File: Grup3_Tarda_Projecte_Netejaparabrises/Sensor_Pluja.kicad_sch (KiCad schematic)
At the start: 5 parts, among them J7 CONEXIOSENSOR, U2 LM393

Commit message: canvis reles
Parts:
- RPOT1: footprint Resistor_SMD:R_0805_2012Metric_Pad1.20x1.40mm_HandSolder -> Projecte:TRIM_3362P-1-103
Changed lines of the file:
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@@
       (effects (font (size 1.27 1.27)) (justify right))
     )
-    (property "Footprint" "Resistor_SMD:R_0805_2012Metric_Pad1.20x1.40mm_HandSolder" (at 110.744 106.68 0)
+    (property "Footprint" "Projecte:TRIM_3362P-1-103" (at 110.744 106.68 0)
       (effects (font (size 1.27 1.27)) hide)
     )

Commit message: Layout 3
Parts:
- CDesOpam1: footprint Capacitor_SMD:CP_Elec_4x3 -> Capacitor_SMD:C_0805_2012Metric
- RPOT1: footprint Projecte:TRIM_3362P-1-103 -> POTENCIOMETRE:TRIM_3362P-1-103
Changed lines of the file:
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@@
   (title_block
     (title "Projecte Netejaparabrises - Grup 4 Tarda")
-    (date "2023-04-12")
-    (rev "v1.2.12042023")
+    (date "2023-04-05")
+    (rev "v1.1.05042023")
   )
   (junction (at 110.744 99.06) (diameter 0) (color 0 0 0 0)
@@
       (effects (font (size 1.27 1.27)) (justify right))
     )
-    (property "Footprint" "Projecte:TRIM_3362P-1-103" (at 110.744 106.68 0)
+    (property "Footprint" "POTENCIOMETRE:TRIM_3362P-1-103" (at 110.744 106.68 0)
       (effects (font (size 1.27 1.27)) hide)
     )
@@
       (effects (font (size 1.27 1.27)) (justify left))
     )
-    (property "Footprint" "Capacitor_SMD:CP_Elec_4x3" (at 177.4952 107.442 0)
-      (effects (font (size 1.27 1.27)) hide)
-    )
+    (property "Footprint" "Capacitor_SMD:C_0805_2012Metric" (at 177.4952 107.442 0)
+      (effects (font (size 1.27 1.27)) hide)
+    )

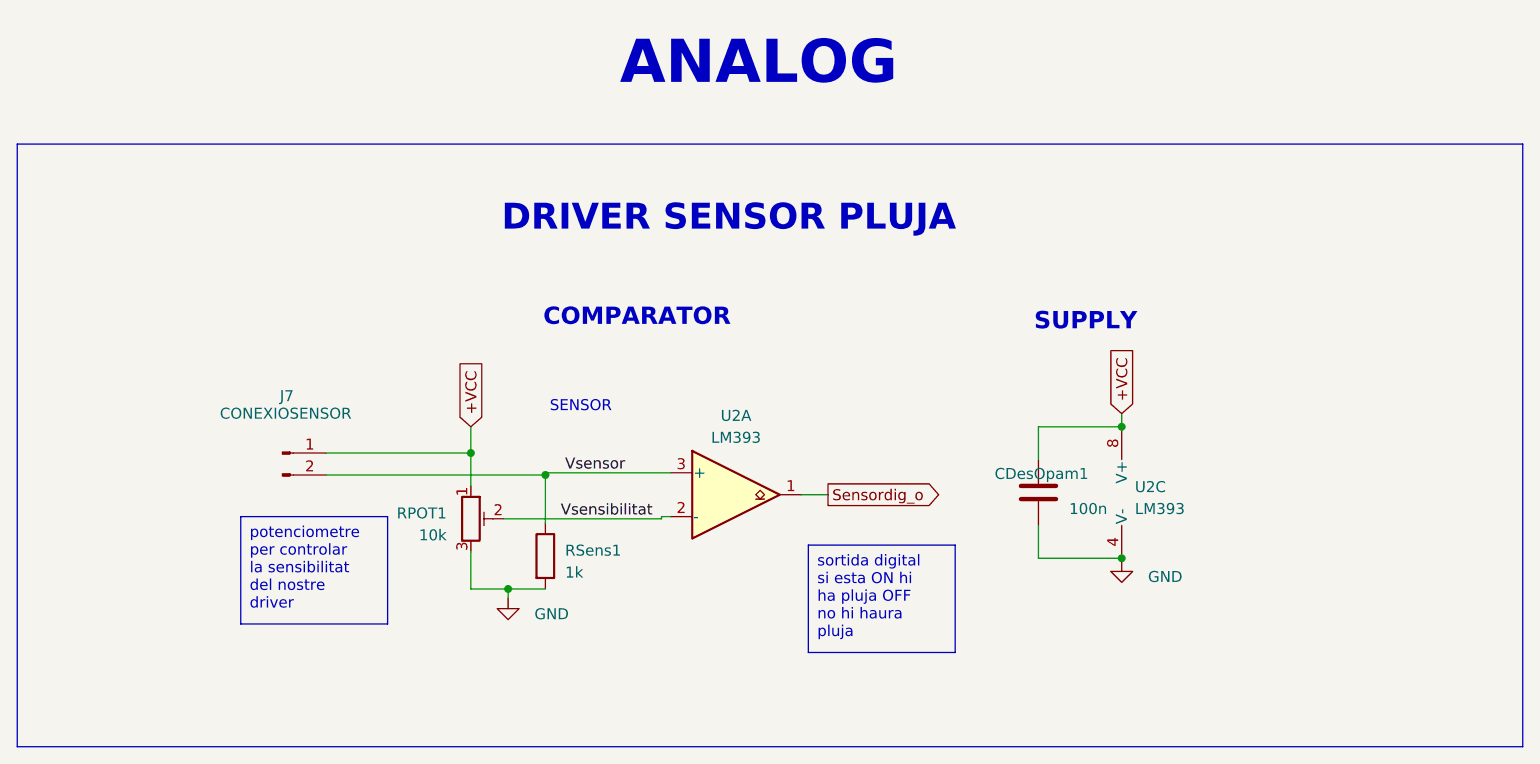
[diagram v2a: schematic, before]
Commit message: canvis divisor sensor de pluja, node vbat protegit, connector de motors, README
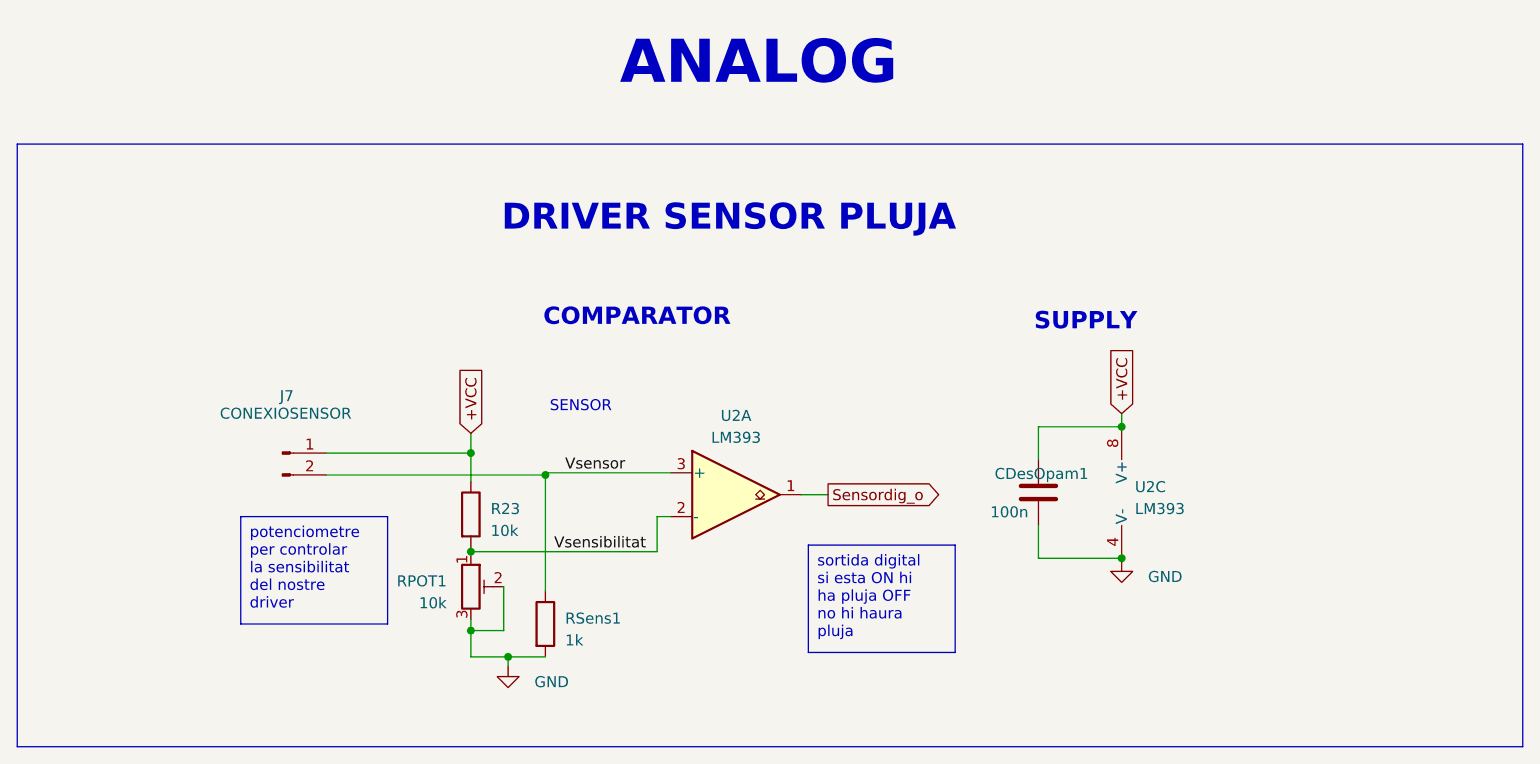
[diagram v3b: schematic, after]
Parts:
- added R23: 10k, Resistor_SMD:R_0805_2012Metric_Pad1.20x1.40mm_HandSolder, symbol Device:R
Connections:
- net +VCC: now also R23.1; no longer RPOT1.1
- net GND: now also RPOT1.2
- net Vsensibilitat: now also RPOT1.1, R23.2; no longer RPOT1.2
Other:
- moved on the sheet: RPOT1, RSens1
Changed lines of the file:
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@@
   (junction (at 110.744 99.06) (diameter 0) (color 0 0 0 0)
   )
+  (junction (at 110.744 119.634) (diameter 0) (color 0 0 0 0)
+  )
   (junction (at 119.38 101.6) (diameter 0) (color 0 0 0 0)
   )
@@
   (junction (at 186.182 111.252) (diameter 0) (color 0 0 0 0)
   )
-  (junction (at 115.062 114.808) (diameter 0) (color 0 0 0 0)
-  )
-  (wire (pts (xy 93.98 99.06) (xy 110.744 99.06))
-    (stroke (width 0) (type default))
-  )
-  (wire (pts (xy 115.062 114.808) (xy 119.38 114.808))
+  (junction (at 110.744 110.49) (diameter 0) (color 0 0 0 0)
+  )
+  (junction (at 115.062 122.682) (diameter 0) (color 0 0 0 0)
+  )
+  (wire (pts (xy 115.062 122.682) (xy 119.38 122.682))
+    (stroke (width 0) (type default))
+  )
+  (wire (pts (xy 114.554 114.554) (xy 114.554 119.634))
     (stroke (width 0) (type default))
   )
@@
     (stroke (width 0) (type default))
   )
-  (wire (pts (xy 110.744 96.012) (xy 110.744 99.06))
+  (wire (pts (xy 110.744 96.774) (xy 110.744 99.06))
     (stroke (width 0) (type default))
   )
@@
     (stroke (width 0) (type default))
   )
-  (wire (pts (xy 115.062 114.808) (xy 115.062 115.824))
-    (stroke (width 0) (type default))
-  )
-  (wire (pts (xy 132.842 106.68) (xy 114.554 106.68))
-    (stroke (width 0) (type default))
-  )
-  (wire (pts (xy 110.744 114.808) (xy 115.062 114.808))
-    (stroke (width 0) (type default))
-  )
-  (wire (pts (xy 132.842 106.426) (xy 132.842 106.68))
-    (stroke (width 0) (type default))
-  )
-  (wire (pts (xy 110.744 110.49) (xy 110.744 114.808))
+  (wire (pts (xy 115.062 122.682) (xy 115.062 123.698))
+    (stroke (width 0) (type default))
+  )
+  (wire (pts (xy 110.744 99.06) (xy 93.98 99.06))
+    (stroke (width 0) (type default))
+  )
+  (wire (pts (xy 110.744 110.49) (xy 132.334 110.49))
+    (stroke (width 0) (type default))
+  )
+  (wire (pts (xy 110.744 122.682) (xy 115.062 122.682))
+    (stroke (width 0) (type default))
+  )
+  (wire (pts (xy 110.744 99.06) (xy 110.744 102.362))
+    (stroke (width 0) (type default))
+  )
+  (wire (pts (xy 110.744 119.634) (xy 114.554 119.634))
+    (stroke (width 0) (type default))
+  )
+  (wire (pts (xy 132.334 106.426) (xy 132.334 110.49))
+    (stroke (width 0) (type default))
+  )
+  (wire (pts (xy 110.744 118.364) (xy 110.744 119.634))
     (stroke (width 0) (type default))
   )
@@
     (stroke (width 0) (type default))
   )
-  (wire (pts (xy 119.38 101.6) (xy 119.38 107.188))
+  (wire (pts (xy 110.744 109.982) (xy 110.744 110.49))
+    (stroke (width 0) (type default))
+  )
+  (wire (pts (xy 119.38 101.6) (xy 119.38 115.062))
     (stroke (width 0) (type default))
   )
@@
     (stroke (width 0) (type default))
   )
-  (wire (pts (xy 132.842 106.426) (xy 133.858 106.426))
-    (stroke (width 0) (type default))
-  )
-  (wire (pts (xy 110.744 99.06) (xy 110.744 102.87))
+  (wire (pts (xy 132.334 106.426) (xy 133.858 106.426))
+    (stroke (width 0) (type default))
+  )
+  (wire (pts (xy 110.744 119.634) (xy 110.744 122.682))
     (stroke (width 0) (type default))
   )
@@
   )
   (polyline (pts (xy 232.664 133.096) (xy 58.166 133.096))
+    (stroke (width 0) (type default))
+  )
+  (wire (pts (xy 110.744 110.49) (xy 110.744 110.744))
     (stroke (width 0) (type default))
   )
@@
     (effects (font (size 1.27 1.27)) (justify left bottom))
   )
-  (label "Vsensibilitat" (at 121.158 106.68 0) (fields_autoplaced)
+  (label "Vsensibilitat" (at 120.396 110.49 0) (fields_autoplaced)
     (effects (font (size 1.27 1.27)) (justify left bottom))
   )
-  (global_label "+VCC" (shape input) (at 110.744 96.012 90) (fields_autoplaced)
+  (global_label "+VCC" (shape input) (at 110.744 96.774 90) (fields_autoplaced)
     (effects (font (size 1.27 1.27)) (justify left))
-    (property "Intersheetrefs" "${INTERSHEET_REFS}" (at 110.744 87.9052 90)
+    (property "Intersheetrefs" "${INTERSHEET_REFS}" (at 110.744 88.6672 90)
       (effects (font (size 1.27 1.27)) (justify left) hide)
     )
@@
     )
   )
-  (symbol (lib_id "Device:R") (at 119.38 110.998 0) (unit 1)
-    (in_bom yes) (on_board yes) (dnp no) (fields_autoplaced)
-    (property "Reference" "RSens1" (at 121.666 110.363 0)
-      (effects (font (size 1.27 1.27)) (justify left))
-    )
-    (property "Value" "1k" (at 121.666 112.903 0)
-      (effects (font (size 1.27 1.27)) (justify left))
-    )
-    (property "Footprint" "Resistor_SMD:R_0805_2012Metric_Pad1.20x1.40mm_HandSolder" (at 117.602 110.998 90)
-      (effects (font (size 1.27 1.27)) hide)
-    )
-    (property "Datasheet" "~" (at 119.38 110.998 0)
+  (symbol (lib_id "Device:R") (at 119.38 118.872 0) (unit 1)
+    (in_bom yes) (on_board yes) (dnp no) (fields_autoplaced)
+    (property "Reference" "RSens1" (at 121.666 118.237 0)
+      (effects (font (size 1.27 1.27)) (justify left))
+    )
+    (property "Value" "1k" (at 121.666 120.777 0)
+      (effects (font (size 1.27 1.27)) (justify left))
+    )
+    (property "Footprint" "Resistor_SMD:R_0805_2012Metric_Pad1.20x1.40mm_HandSolder" (at 117.602 118.872 90)
+      (effects (font (size 1.27 1.27)) hide)
+    )
+    (property "Datasheet" "~" (at 119.38 118.872 0)
       (effects (font (size 1.27 1.27)) hide)
     )
@@
     )
   )
-  (symbol (lib_id "Device:R_Potentiometer_Trim") (at 110.744 106.68 0) (unit 1)
-    (in_bom yes) (on_board yes) (dnp no) (fields_autoplaced)
-    (property "Reference" "RPOT1" (at 107.95 106.045 0)
+  (symbol (lib_id "Device:R_Potentiometer_Trim") (at 110.744 114.554 0) (unit 1)
+    (in_bom yes) (on_board yes) (dnp no) (fields_autoplaced)
+    (property "Reference" "RPOT1" (at 107.95 113.919 0)
       (effects (font (size 1.27 1.27)) (justify right))
     )
-    (property "Value" "10k" (at 107.95 108.585 0)
+    (property "Value" "10k" (at 107.95 116.459 0)
       (effects (font (size 1.27 1.27)) (justify right))
     )
-    (property "Footprint" "POTENCIOMETRE:TRIM_3362P-1-103" (at 110.744 106.68 0)
-      (effects (font (size 1.27 1.27)) hide)
-    )
-    (property "Datasheet" "~" (at 110.744 106.68 0)
+    (property "Footprint" "POTENCIOMETRE:TRIM_3362P-1-103" (at 110.744 114.554 0)
+      (effects (font (size 1.27 1.27)) hide)
+    )
+    (property "Datasheet" "~" (at 110.744 114.554 0)
       (effects (font (size 1.27 1.27)) hide)
     )
@@
       (effects (font (size 1.27 1.27)) (justify left))
     )
-    (property "Value" "100n" (at 180.086 105.537 0)
+    (property "Value" "100n" (at 170.942 105.918 0)
       (effects (font (size 1.27 1.27)) (justify left))
     )
@@
         (path "/7ae78f34-680b-4fd9-8391-ce3e1c73c4b5/1911e221-32e7-4aa1-805e-6cbecb9cf221"
           (reference "CDesOpam1") (unit 1)
+        )
+      )
+    )
+  )
+  (symbol (lib_id "Device:R") (at 110.744 106.172 0) (unit 1)
+    (in_bom yes) (on_board yes) (dnp no) (fields_autoplaced)
+    (property "Reference" "R23" (at 113.03 105.537 0)
+      (effects (font (size 1.27 1.27)) (justify left))
+    )
+    (property "Value" "10k" (at 113.03 108.077 0)
+      (effects (font (size 1.27 1.27)) (justify left))
+    )
+    (property "Footprint" "Resistor_SMD:R_0805_2012Metric_Pad1.20x1.40mm_HandSolder" (at 108.966 106.172 90)
+      (effects (font (size 1.27 1.27)) hide)
+    )
+    (property "Datasheet" "~" (at 110.744 106.172 0)
+      (effects (font (size 1.27 1.27)) hide)
+    )
+    (pin "1")
+    (pin "2")
+    (instances
+      (project "Grup3_Tarda_Projecte_Netejaparabrises"
+        (path "/7ae78f34-680b-4fd9-8391-ce3e1c73c4b5/1911e221-32e7-4aa1-805e-6cbecb9cf221"
+          (reference "R23") (unit 1)
         )
       )
@@
     )
   )
-  (symbol (lib_id "power:GND") (at 115.062 115.824 0) (unit 1)
-    (in_bom yes) (on_board yes) (dnp no) (fields_autoplaced)
-    (property "Reference" "#PWR017" (at 115.062 122.174 0)
-      (effects (font (size 1.27 1.27)) hide)
-    )
-    (property "Value" "GND" (at 118.11 117.729 0)
-      (effects (font (size 1.27 1.27)) (justify left))
-    )
-    (property "Footprint" "" (at 115.062 115.824 0)
-      (effects (font (size 1.27 1.27)) hide)
-    )
-    (property "Datasheet" "" (at 115.062 115.824 0)
-      (effects (font (size 1.27 1.27)) hide)
-    )
+  (symbol (lib_id "power:GND") (at 115.062 123.698 0) (unit 1)
+    (in_bom yes) (on_board yes) (dnp no) (fields_autoplaced)
+    (property "Reference" "#PWR017" (at 115.062 130.048 0)
+      (effects (font (size 1.27 1.27)) hide)
+    )
+    (property "Value" "GND" (at 118.11 125.603 0)
+      (effects (font (size 1.27 1.27)) (justify left))
+    )
+    (property "Footprint" "" (at 115.062 123.698 0)
+      (effects (font (size 1.27 1.27)) hide)
+    )
+    (property "Datasheet" "" (at 115.062 123.698 0)
+      (effects (font (size 1.27 1.27)) hide)
+    )

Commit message: routing v1 sense acabar
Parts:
- CDesOpam1: footprint Capacitor_SMD:C_0805_2012Metric -> Capacitor_THT:C_Disc_D3.0mm_W1.6mm_P2.50mm
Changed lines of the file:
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@@
       (effects (font (size 1.27 1.27)) (justify left))
     )
-    (property "Footprint" "Capacitor_SMD:C_0805_2012Metric" (at 177.4952 107.442 0)
+    (property "Footprint" "Capacitor_THT:C_Disc_D3.0mm_W1.6mm_P2.50mm" (at 177.4952 107.442 0)
       (effects (font (size 1.27 1.27)) hide)
     )

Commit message: placing rooting
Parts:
- CDesOpam1: footprint Capacitor_THT:C_Disc_D3.0mm_W1.6mm_P2.50mm -> Capacitor_SMD:C_0805_2012Metric_Pad1.18x1.45mm_HandSolder
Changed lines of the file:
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@@
       (effects (font (size 1.27 1.27)) (justify left))
     )
-    (property "Footprint" "Capacitor_THT:C_Disc_D3.0mm_W1.6mm_P2.50mm" (at 177.4952 107.442 0)
+    (property "Footprint" "Capacitor_SMD:C_0805_2012Metric_Pad1.18x1.45mm_HandSolder" (at 177.4952 107.442 0)
       (effects (font (size 1.27 1.27)) hide)
     )

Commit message: definitiu
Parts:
- J7: footprint Connector_PinSocket_2.54mm:PinSocket_1x02_P2.54mm_Vertical -> Connector_PinHeader_2.54mm:PinHeader_1x02_P2.54mm_Vertical
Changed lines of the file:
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@@
   (title_block
     (title "Projecte Netejaparabrises - Grup 4 Tarda")
-    (date "2023-04-20")
+    (date "2023-04-27")
     (rev "v1.3.20042023")
   )
@@
       (effects (font (size 1.27 1.27)))
     )
-    (property "Footprint" "Connector_PinSocket_2.54mm:PinSocket_1x02_P2.54mm_Vertical" (at 88.9 99.06 0)
+    (property "Footprint" "Connector_PinHeader_2.54mm:PinHeader_1x02_P2.54mm_Vertical" (at 88.9 99.06 0)
       (effects (font (size 1.27 1.27)) hide)
     )
